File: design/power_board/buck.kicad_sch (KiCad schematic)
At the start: 9 parts, among them U1 LV2862YDDCR

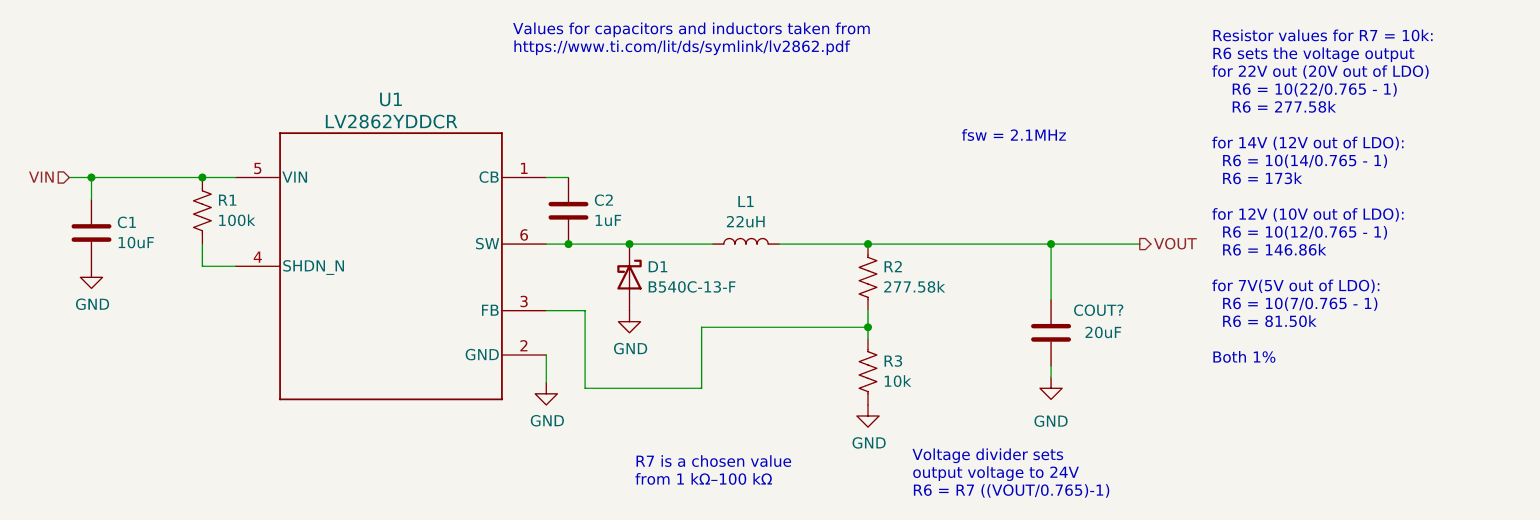
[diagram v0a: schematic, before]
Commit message: Changed diode footprints
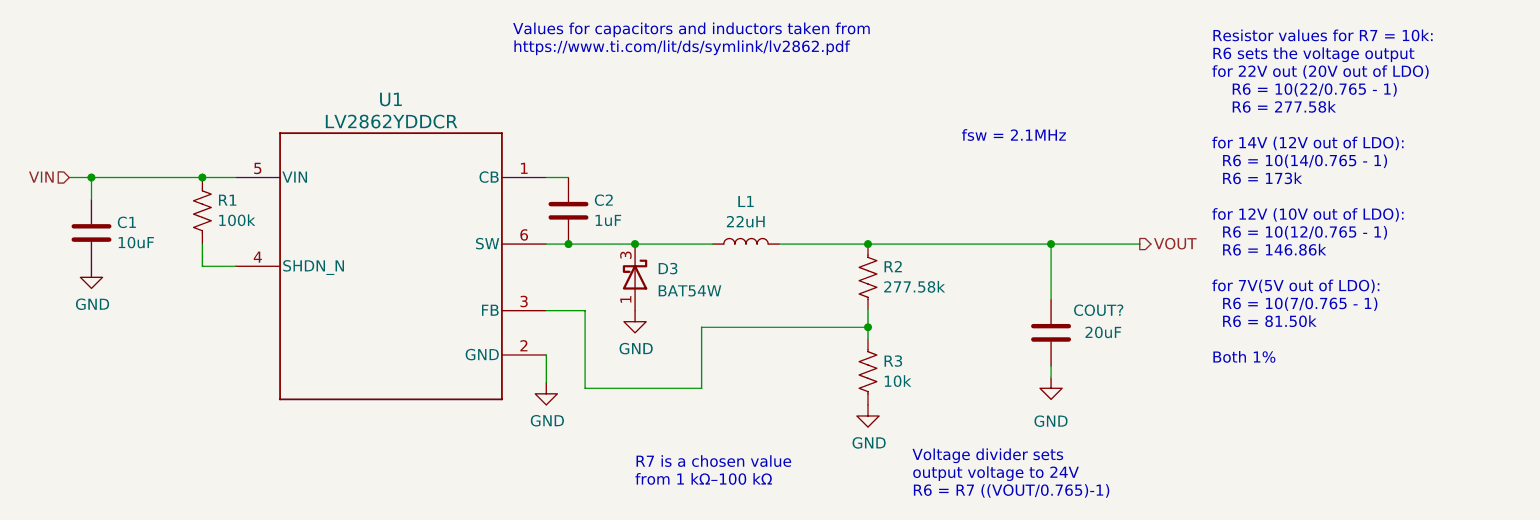
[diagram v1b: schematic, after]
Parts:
- removed D1: B540C-13-F, Diode_THT:D_DO-41_SOD81_P10.16mm_Horizontal, symbol Device:D_Schottky
- added D3: BAT54W, Package_TO_SOT_SMD:SOT-323_SC-70, symbol Diode:BAT54W
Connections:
- net GND: now also D3.1 (A)
- net at C2.1, L1.1, U1.6 (SW): now also D3.3 (K)
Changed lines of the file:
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@@
   (junction (at 86.36 87.63) (diameter 0) (color 0 0 0 0)
   )
+  (junction (at 148.59 95.25) (diameter 0) (color 0 0 0 0)
+  )
   (junction (at 99.06 87.63) (diameter 0) (color 0 0 0 0)
   )
@@
   (junction (at 175.26 104.775) (diameter 0) (color 0 0 0 0)
   )
-  (junction (at 147.955 95.25) (diameter 0) (color 0 0 0 0)
-  )
   (wire (pts (xy 138.43 102.87) (xy 142.875 102.87))
     (stroke (width 0) (type default))
@@
     (stroke (width 0) (type default))
   )
-  (wire (pts (xy 140.97 95.25) (xy 147.955 95.25))
-    (stroke (width 0) (type default))
-  )
   (wire (pts (xy 138.43 87.63) (xy 140.97 87.63))
     (stroke (width 0) (type default))
@@
     (stroke (width 0) (type default))
   )
-  (wire (pts (xy 147.955 95.25) (xy 157.48 95.25))
+  (wire (pts (xy 140.97 95.25) (xy 148.59 95.25))
     (stroke (width 0) (type default))
   )
@@
   )
   (wire (pts (xy 99.06 97.79) (xy 102.87 97.79))
+    (stroke (width 0) (type default))
+  )
+  (wire (pts (xy 148.59 95.25) (xy 157.48 95.25))
     (stroke (width 0) (type default))
   )
@@
     )
   )
-  (symbol (lib_id "Device:D_Schottky") (at 147.955 99.06 270) (unit 1)
-    (in_bom yes) (on_board yes) (dnp no)
-    (property "Reference" "D1" (at 149.987 97.8916 90)
-      (effects (font (size 1.27 1.27)) (justify left))
-    )
-    (property "Value" "B540C-13-F" (at 149.987 100.203 90)
-      (effects (font (size 1.27 1.27)) (justify left))
-    )
-    (property "Footprint" "Diode_THT:D_DO-41_SOD81_P10.16mm_Horizontal" (at 147.955 99.06 0)
-      (effects (font (size 1.27 1.27)) hide)
-    )
-    (property "Datasheet" "~" (at 147.955 99.06 0)
-      (effects (font (size 1.27 1.27)) hide)
-    )
-    (pin "1")
-    (pin "2")
-    (instances
-      (project "buck_fixed"
-        (path "/5a149a99-7ef6-4309-ac70-ee1dc896f69a"
-          (reference "D1") (unit 1)
-        )
-      )
-      (project "power_board"
-        (path "/8a849c59-59c0-42e0-a511-c33c123656fd/00000000-0000-0000-0000-00006153da18"
-          (reference "D1") (unit 1)
-        )
-      )
-    )
-  )
   (symbol (lib_id "Device:L") (at 161.29 95.25 90) (unit 1)
     (in_bom yes) (on_board yes) (dnp no)
@@
     )
   )
-  (symbol (lib_id "power:GND") (at 147.955 102.87 0) (unit 1)
-    (in_bom yes) (on_board yes) (dnp no)
-    (property "Reference" "#PWR0102" (at 147.955 109.22 0)
-      (effects (font (size 1.27 1.27)) hide)
-    )
-    (property "Value" "GND" (at 148.082 107.2642 0)
+  (symbol (lib_id "power:GND") (at 148.59 102.87 0) (unit 1)
+    (in_bom yes) (on_board yes) (dnp no)
+    (property "Reference" "#PWR0102" (at 148.59 109.22 0)
+      (effects (font (size 1.27 1.27)) hide)
+    )
+    (property "Value" "GND" (at 148.717 107.2642 0)
       (effects (font (size 1.27 1.27)))
     )
-    (property "Footprint" "" (at 147.955 102.87 0)
-      (effects (font (size 1.27 1.27)) hide)
-    )
-    (property "Datasheet" "" (at 147.955 102.87 0)
+    (property "Footprint" "" (at 148.59 102.87 0)
+      (effects (font (size 1.27 1.27)) hide)
+    )
+    (property "Datasheet" "" (at 148.59 102.87 0)
       (effects (font (size 1.27 1.27)) hide)
     )
@@
         )
       )
+    )
+  )
+  (symbol (lib_id "Diode:BAT54W") (at 148.59 99.06 270) (unit 1)
+    (in_bom yes) (on_board yes) (dnp no) (fields_autoplaced)
+    (property "Reference" "D3" (at 151.13 98.1075 90)
+      (effects (font (size 1.27 1.27)) (justify left))
+    )
+    (property "Value" "BAT54W" (at 151.13 100.6475 90)
+      (effects (font (size 1.27 1.27)) (justify left))
+    )
+    (property "Footprint" "Package_TO_SOT_SMD:SOT-323_SC-70" (at 144.145 99.06 0)
+      (effects (font (size 1.27 1.27)) hide)
+    )
+    (property "Datasheet" "https://assets.nexperia.com/documents/data-sheet/BAT54W_SER.pdf" (at 148.59 99.06 0)
+      (effects (font (size 1.27 1.27)) hide)
+    )
+    (pin "1")
+    (pin "2")
+    (pin "3")
+    (instances
+      (project "power_board"
+        (path "/8a849c59-59c0-42e0-a511-c33c123656fd/00000000-0000-0000-0000-00006153da18"
+          (reference "D3") (unit 1)
+        )
+      )

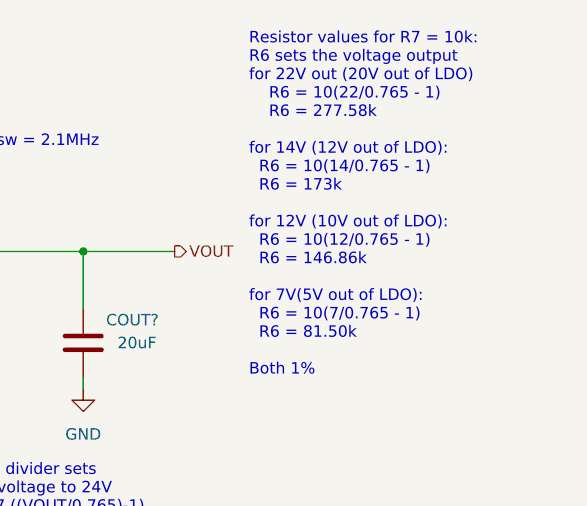
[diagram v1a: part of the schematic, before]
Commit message: Updated LED calculations, diodes, LDO symbol
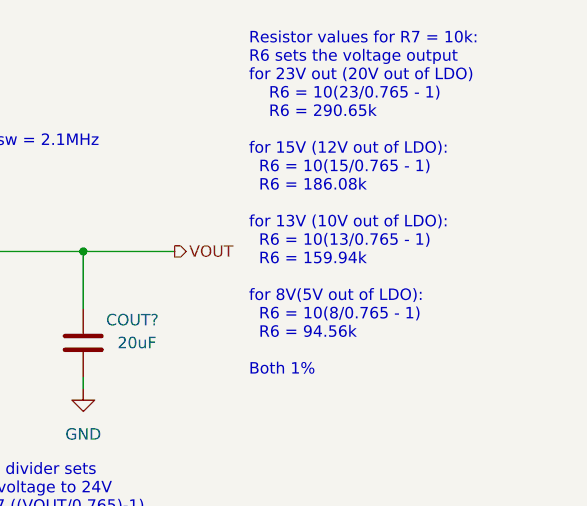
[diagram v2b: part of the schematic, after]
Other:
- note added: "Resistor values for R7 = 10k: R6 sets the voltage output for 23V out (20V out of LDO) R6 = 10(23/0.765 - 1) R6 = 290.65k for 15V (12V out of LDO): R6 = 10(15/0.765 - 1) R6 = 186.08k for 13V (10V out of LDO): R6 = 10(13/0.765 - 1) R6 = 159.94k for 8V(5V out of LDO): R6 = 10(8/0.765 - 1) R6 = 94.56k Both 1%"
- note removed: "Resistor values for R7 = 10k: R6 sets the voltage output for 22V out (20V out of LDO) R6 = 10(22/0.765 - 1) R6 = 277.58k for 14V (12V out of LDO): R6 = 10(14/0.765 - 1) R6 = 173k for 12V (10V out of LDO): R6 = 10(12/0.765 - 1) R6 = 146.86k for 7V(5V out of LDO): R6 = 10(7/0.765 - 1) R6 = 81.50k Both 1%"
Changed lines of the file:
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@@
     (effects (font (size 1.27 1.27)) (justify left bottom))
   )
-  (text "Resistor values for R7 = 10k:\nR6 sets the voltage output\nfor 22V out (20V out of LDO)\n	R6 = 10(22/0.765 - 1)\n	R6 = 277.58k\n\nfor 14V (12V out of LDO):\n  R6 = 10(14/0.765 - 1)\n  R6 = 173k\n\nfor 12V (10V out of LDO):\n  R6 = 10(12/0.765 - 1)\n  R6 = 146.86k\n\nfor 7V(5V out of LDO):\n  R6 = 10(7/0.765 - 1)\n  R6 = 81.50k\n\nBoth 1%"
+  (text "Resistor values for R7 = 10k:\nR6 sets the voltage output\nfor 23V out (20V out of LDO)\n	R6 = 10(23/0.765 - 1)\n	R6 = 290.65k\n\nfor 15V (12V out of LDO):\n  R6 = 10(15/0.765 - 1)\n  R6 = 186.08k\n\nfor 13V (10V out of LDO):\n  R6 = 10(13/0.765 - 1)\n  R6 = 159.94k\n\nfor 8V(5V out of LDO):\n  R6 = 10(8/0.765 - 1)\n  R6 = 94.56k\n\nBoth 1%"
     (at 214.63 109.22 0)
     (effects (font (size 1.27 1.27)) (justify left bottom))
@@
       (project "power_board"
         (path "/8a849c59-59c0-42e0-a511-c33c123656fd/00000000-0000-0000-0000-00006153da18"
-          (reference "COUT1") (unit 1)
-        )
-      )
+          (reference "C3") (unit 1)
+        )
+      )

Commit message: Inductor footprint
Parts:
- L1: footprint Inductor_SMD:L_0805_2012Metric_Pad1.15x1.40mm_HandSolder -> Inductor_SMD:L_Bourns-SRU1028_10.0x10.0mm
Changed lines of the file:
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@@
       (effects (font (size 1.27 1.27)))
     )
-    (property "Footprint" "Inductor_SMD:L_0805_2012Metric_Pad1.15x1.40mm_HandSolder" (at 161.29 95.25 0)
+    (property "Footprint" "Inductor_SMD:L_Bourns-SRU1028_10.0x10.0mm" (at 161.29 95.25 0)
       (effects (font (size 1.27 1.27)) hide)
     )

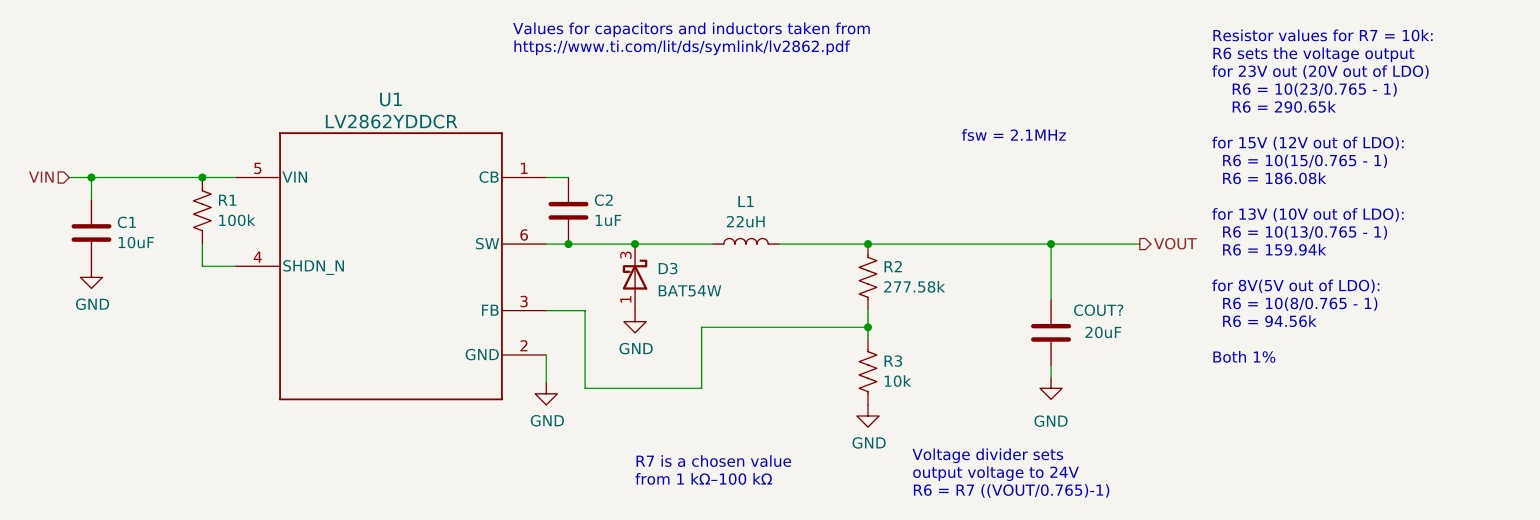
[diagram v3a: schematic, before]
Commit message: Updated buck diode
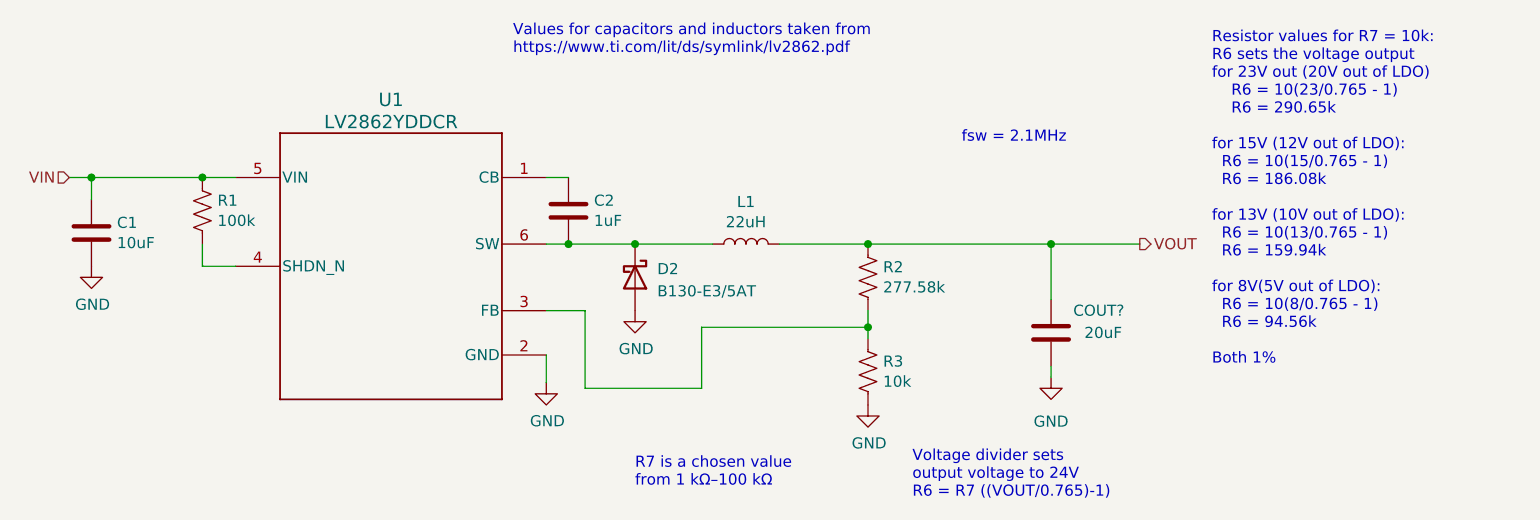
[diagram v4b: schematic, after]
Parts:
- removed D3: BAT54W, Package_TO_SOT_SMD:SOT-323_SC-70, symbol Diode:BAT54W
- added D2: B130-E3/5AT, Diode_SMD:D_SMA, symbol Diode:B130-E3
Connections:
- net GND: now also D2.2 (A)
- net at C2.1, L1.1, U1.6 (SW): now also D2.1 (K)
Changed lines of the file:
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@@
   (junction (at 86.36 87.63) (diameter 0) (color 0 0 0 0)
   )
+  (junction (at 99.06 87.63) (diameter 0) (color 0 0 0 0)
+  )
+  (junction (at 175.26 95.25) (diameter 0) (color 0 0 0 0)
+  )
   (junction (at 148.59 95.25) (diameter 0) (color 0 0 0 0)
   )
-  (junction (at 99.06 87.63) (diameter 0) (color 0 0 0 0)
-  )
-  (junction (at 175.26 95.25) (diameter 0) (color 0 0 0 0)
-  )
   (junction (at 140.97 95.25) (diameter 0) (color 0 0 0 0)
   )
@@
     (stroke (width 0) (type default))
   )
+  (wire (pts (xy 148.59 95.25) (xy 157.48 95.25))
+    (stroke (width 0) (type default))
+  )
   (wire (pts (xy 138.43 95.25) (xy 140.97 95.25))
     (stroke (width 0) (type default))
@@
     (stroke (width 0) (type default))
   )
+  (wire (pts (xy 138.43 107.95) (xy 138.43 111.125))
+    (stroke (width 0) (type default))
+  )
+  (wire (pts (xy 156.21 104.775) (xy 175.26 104.775))
+    (stroke (width 0) (type default))
+  )
+  (wire (pts (xy 175.26 102.87) (xy 175.26 104.775))
+    (stroke (width 0) (type default))
+  )
+  (wire (pts (xy 142.875 111.76) (xy 156.21 111.76))
+    (stroke (width 0) (type default))
+  )
+  (wire (pts (xy 175.26 95.25) (xy 196.215 95.25))
+    (stroke (width 0) (type default))
+  )
+  (wire (pts (xy 99.06 97.79) (xy 102.87 97.79))
+    (stroke (width 0) (type default))
+  )
   (wire (pts (xy 140.97 95.25) (xy 148.59 95.25))
-    (stroke (width 0) (type default))
-  )
-  (wire (pts (xy 138.43 107.95) (xy 138.43 111.125))
-    (stroke (width 0) (type default))
-  )
-  (wire (pts (xy 156.21 104.775) (xy 175.26 104.775))
-    (stroke (width 0) (type default))
-  )
-  (wire (pts (xy 175.26 102.87) (xy 175.26 104.775))
-    (stroke (width 0) (type default))
-  )
-  (wire (pts (xy 142.875 111.76) (xy 156.21 111.76))
-    (stroke (width 0) (type default))
-  )
-  (wire (pts (xy 175.26 95.25) (xy 196.215 95.25))
-    (stroke (width 0) (type default))
-  )
-  (wire (pts (xy 99.06 97.79) (xy 102.87 97.79))
-    (stroke (width 0) (type default))
-  )
-  (wire (pts (xy 148.59 95.25) (xy 157.48 95.25))
     (stroke (width 0) (type default))
   )
@@
       (effects (font (size 1.27 1.27)) hide)
     )
-    (property "Datasheet" "~" (at 161.29 95.25 0)
+    (property "Datasheet" "SRU1028-220Y" (at 161.29 95.25 0)
       (effects (font (size 1.27 1.27)) hide)
     )
@@
     )
   )
+  (symbol (lib_id "Diode:B130-E3") (at 148.59 99.06 270) (unit 1)
+    (in_bom yes) (on_board yes) (dnp no) (fields_autoplaced)
+    (property "Reference" "D2" (at 151.13 98.1075 90)
+      (effects (font (size 1.27 1.27)) (justify left))
+    )
+    (property "Value" "B130-E3/5AT" (at 151.13 100.6475 90)
+      (effects (font (size 1.27 1.27)) (justify left))
+    )
+    (property "Footprint" "Diode_SMD:D_SMA" (at 144.145 99.06 0)
+      (effects (font (size 1.27 1.27)) hide)
+    )
+    (property "Datasheet" "http://www.vishay.com/docs/88946/b120.pdf" (at 148.59 99.06 0)
+      (effects (font (size 1.27 1.27)) hide)
+    )
+    (pin "1")
+    (pin "2")
+    (instances
+      (project "power_board"
+        (path "/8a849c59-59c0-42e0-a511-c33c123656fd/00000000-0000-0000-0000-00006153da18"
+          (reference "D2") (unit 1)
+        )
+      )
+    )
+  )
   (symbol (lib_id "Device:R_US") (at 175.26 109.855 0) (unit 1)
     (in_bom yes) (on_board yes) (dnp no)
@@
         )
       )
-    )
-  )
-  (symbol (lib_id "Diode:BAT54W") (at 148.59 99.06 270) (unit 1)
-    (in_bom yes) (on_board yes) (dnp no) (fields_autoplaced)
-    (property "Reference" "D3" (at 151.13 98.1075 90)
-      (effects (font (size 1.27 1.27)) (justify left))
-    )
-    (property "Value" "BAT54W" (at 151.13 100.6475 90)
-      (effects (font (size 1.27 1.27)) (justify left))
-    )
-    (property "Footprint" "Package_TO_SOT_SMD:SOT-323_SC-70" (at 144.145 99.06 0)
-      (effects (font (size 1.27 1.27)) hide)
-    )
-    (property "Datasheet" "https://assets.nexperia.com/documents/data-sheet/BAT54W_SER.pdf" (at 148.59 99.06 0)
-      (effects (font (size 1.27 1.27)) hide)
-    )
-    (pin "1")
-    (pin "2")
-    (pin "3")
-    (instances
-      (project "power_board"
-        (path "/8a849c59-59c0-42e0-a511-c33c123656fd/00000000-0000-0000-0000-00006153da18"
-          (reference "D3") (unit 1)
-        )
-      )
